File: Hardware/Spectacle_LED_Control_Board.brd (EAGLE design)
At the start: 25.4 x 55.9 mm, 43 parts, among them J3 USB-MICROB, J4 AUDIO-JACK3, J8 AUDIO-JACK3, U1 CY8C4245LQI-483, U2 3.3V, U4 SN74LVC1G66, U5 SN74LVC1G66

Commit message: Routed and ready to check
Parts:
- moved U5 0.38 mm to (16.3, 11.4)
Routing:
- net 3.3V: track 41.6 -> 20.2 mm, vias 1 -> 5
- net GND: track 44.9 -> 30.8 mm, vias 2 -> 4
- net LED: track 0.00 -> 14.0 mm, vias 0 -> 2
- net XRES: track 24.8 -> 36.2 mm
- net BTN: track 4.85 -> 6.84 mm
- net N$5: track 0.00 -> 1.66 mm
- net LED_1: track 19.5 -> 18.9 mm

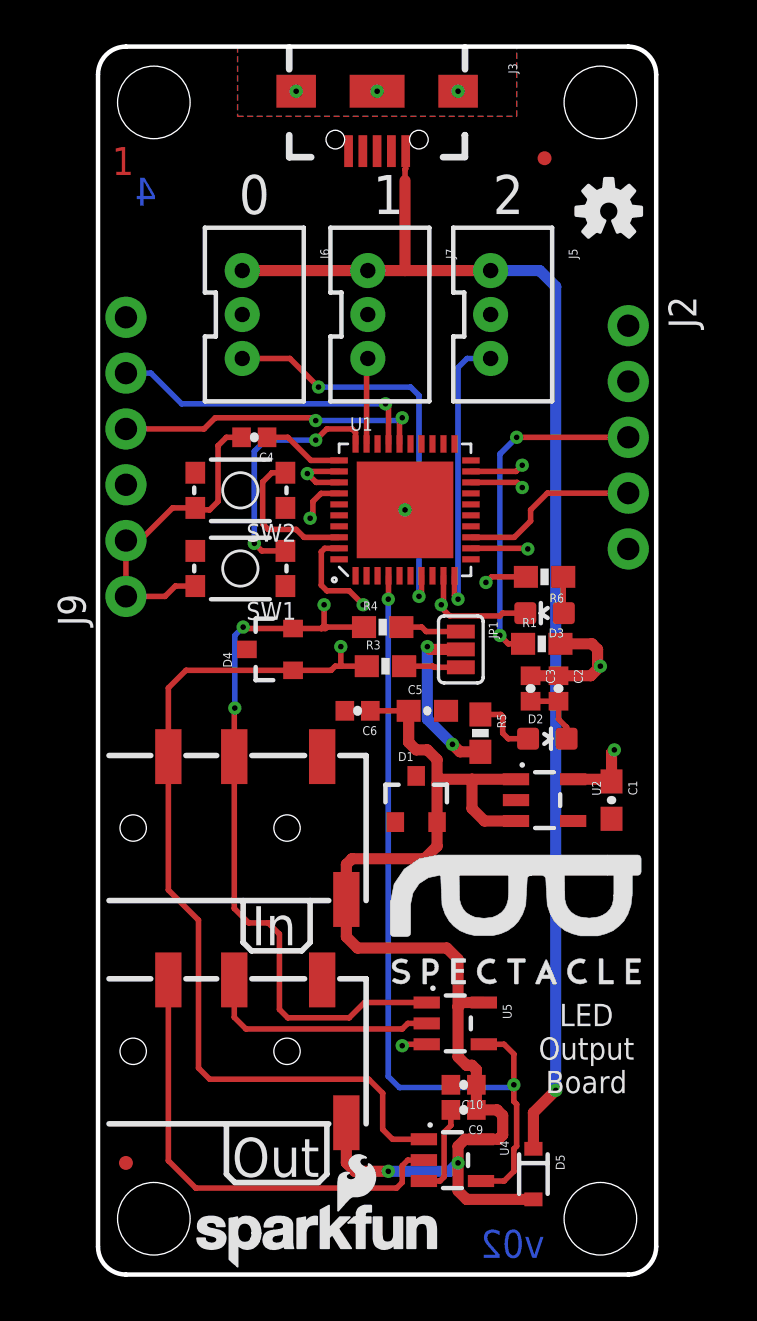
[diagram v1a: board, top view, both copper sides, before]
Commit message: moving caps
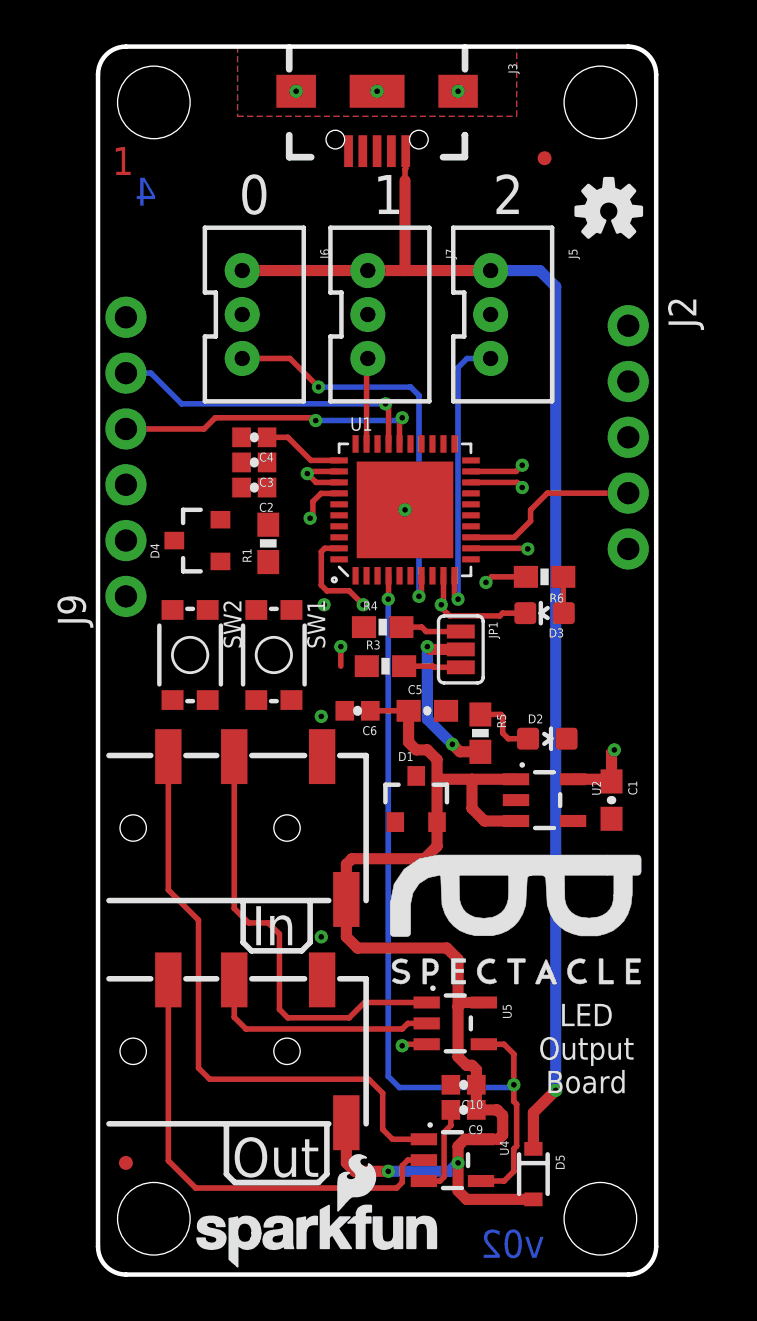
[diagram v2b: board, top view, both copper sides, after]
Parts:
- moved C2 16.6 mm to (7.11, 35.8), turned to 180 degrees
- moved C3 16.2 mm to (7.11, 37.0), turned to 180 degrees
- moved R1 13.3 mm to (7.75, 33.3), turned to 90 degrees
- moved SW2 7.83 mm to (4.19, 28.2), turned to 270 degrees
- moved D4 5.95 mm to (4.57, 33.4)
- moved SW1 4.22 mm to (8.00, 28.2), turned to 270 degrees
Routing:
- net XRES: track 36.2 -> 0.00 mm, vias 4 -> 0
- net GND: track 30.8 -> 13.0 mm, vias 4 -> 6
- net SDA: track 50.3 -> 37.5 mm, vias 4 -> 2
- net SCL: track 58.4 -> 45.8 mm
- net BTN: track 6.84 -> 0.00 mm
- net 3.3V: track 20.2 -> 14.3 mm, vias 5 -> 4

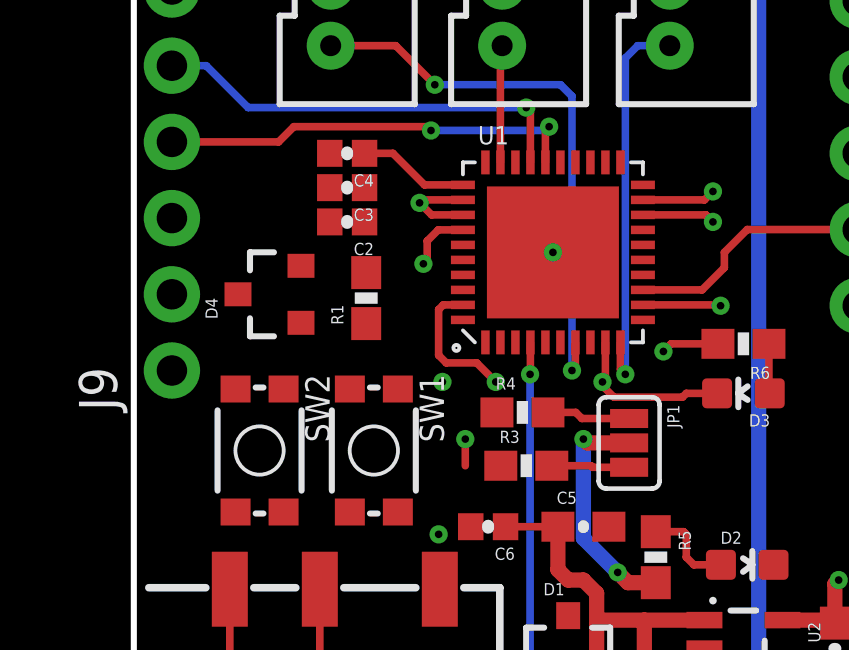
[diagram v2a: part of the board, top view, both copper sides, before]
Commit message: Moving caps
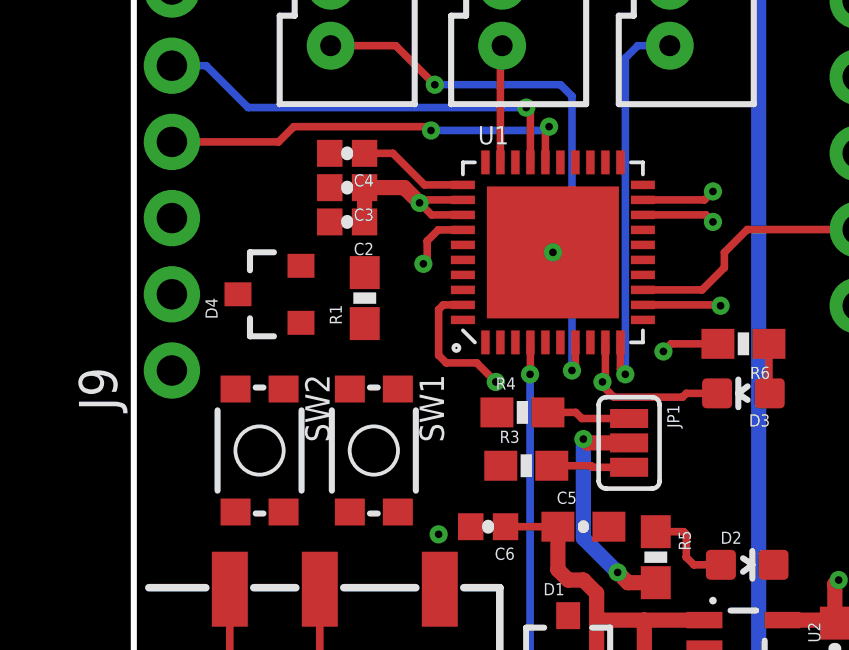
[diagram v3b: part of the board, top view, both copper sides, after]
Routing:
- net 3.3V: track 14.3 -> 17.5 mm
- net SCL: track 45.8 -> 44.9 mm, vias 2 -> 1
- net SDA: vias 2 -> 1
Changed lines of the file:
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@@
 <?xml version="1.0" encoding="utf-8"?>
 <!DOCTYPE eagle SYSTEM "eagle.dtd">
-<eagle version="7.6.0">
+<eagle version="7.3.0">
 <drawing>
 <settings>
@@
 <layers>
 <layer number="1" name="Top" color="4" fill="1" visible="yes" active="yes"/>
-<layer number="2" name="Route2" color="1" fill="3" visible="yes" active="yes"/>
-<layer number="15" name="Route15" color="4" fill="6" visible="yes" active="yes"/>
+<layer number="2" name="Route2" color="1" fill="3" visible="no" active="yes"/>
+<layer number="15" name="Route15" color="4" fill="6" visible="no" active="yes"/>
 <layer number="16" name="Bottom" color="1" fill="1" visible="yes" active="yes"/>
 <layer number="17" name="Pads" color="2" fill="1" visible="yes" active="yes"/>
@@
 <layer number="47" name="Measures" color="7" fill="1" visible="no" active="yes"/>
 <layer number="51" name="tDocu" color="6" fill="1" visible="yes" active="yes"/>
-<layer number="52" name="bDocu" color="7" fill="1" visible="no" active="yes"/>
+<layer number="52" name="bDocu" color="7" fill="1" visible="no" active="no"/>
 <layer number="48" name="Document" color="7" fill="1" visible="no" active="no"/>
 <layer number="49" name="Reference" color="7" fill="1" visible="no" active="no"/>
@@
 <attribute name="PROD_ID" value="VREG-12457" x="20.32" y="21.59" size="1.778" layer="27" font="vector" ratio="15" rot="R270" display="off"/>
 </element>
-<element name="R1" library="SparkFun-Resistors" package="0603-RES" value="10K" x="7.747" y="33.274" rot="R90">
-<attribute name="PROD_ID" value="RES-00824" x="7.747" y="33.274" size="1.778" layer="27" font="vector" ratio="15" rot="R90" display="off"/>
+<element name="R1" library="SparkFun-Resistors" package="0603-RES" value="10K" x="7.697" y="33.274" rot="R90">
+<attribute name="PROD_ID" value="RES-00824" x="7.697" y="33.274" size="1.778" layer="27" font="vector" ratio="15" rot="R90" display="off"/>
 </element>
 <element name="C1" library="SparkFun-Capacitors" package="0603-CAP" value="2.2uF" x="23.368" y="21.59" rot="R270">
@@
 <contactref element="SW1" pad="1"/>
 <contactref element="U1" pad="30"/>
-<wire x1="7.747" y1="32.424" x2="24.13" y2="38.1" width="0" layer="19" extent="1-1"/>
-<wire x1="11.72" y1="37.798" x2="7.747" y2="32.424" width="0" layer="19" extent="1-1"/>
-<wire x1="7.201" y1="30.244" x2="11.72" y2="37.798" width="0" layer="19" extent="1-1"/>
+<wire x1="11.72" y1="37.798" x2="24.13" y2="38.1" width="0" layer="19" extent="1-1"/>
+<wire x1="7.697" y1="32.424" x2="11.72" y2="37.798" width="0" layer="19" extent="1-1"/>
+<wire x1="7.201" y1="30.244" x2="7.697" y2="32.424" width="0" layer="19" extent="1-1"/>
 </signal>
 <signal name="VIN">
@@
 <wire x1="11.557" y1="35.814" x2="11.049" y2="35.306" width="0.254" layer="2"/>
 <wire x1="11.049" y1="35.306" x2="11.049" y2="28.575" width="0.254" layer="2"/>
-<via x="11.049" y="28.575" extent="1-16" drill="0.254"/>
-<wire x1="11.049" y1="28.575" x2="11.049" y2="27.686" width="0.254" layer="1"/>
-<wire x1="11.049" y1="27.686" x2="12.231" y2="27.686" width="0" layer="19" extent="1-1"/>
+<wire x1="12.231" y1="27.686" x2="11.049" y2="28.575" width="0" layer="19" extent="1-2"/>
 <wire x1="5.572" y1="32.451" x2="11.049" y2="35.306" width="0" layer="19" extent="1-2"/>
-<wire x1="3.2" y1="23.57" x2="11.049" y2="27.686" width="0" layer="19" extent="1-1"/>
+<wire x1="3.2" y1="23.57" x2="5.572" y2="32.451" width="0" layer="19" extent="1-1"/>
 </signal>
 <signal name="SDA">
@@
 <wire x1="10.795" y1="36.83" x2="10.287" y2="36.322" width="0.254" layer="2"/>
 <wire x1="10.287" y1="36.322" x2="10.287" y2="30.48" width="0.254" layer="2"/>
-<via x="10.287" y="30.48" extent="1-16" drill="0.254"/>
 <wire x1="14.9559" y1="12.38" x2="12.126" y2="12.38" width="0.254" layer="1"/>
 <wire x1="12.126" y1="12.38" x2="11.43" y2="11.684" width="0.254" layer="1"/>
@@
 <wire x1="21.6201" y1="22.54" x2="23.268" y2="22.54" width="0.508" layer="1"/>
 <wire x1="23.268" y1="22.54" x2="23.368" y2="22.44" width="0.508" layer="1"/>
-<wire x1="22.86" y1="27.686" x2="22.86" y2="27.686" width="0" layer="19" extent="1-16"/>
-<wire x1="7.747" y1="34.124" x2="22.479" y2="28.702" width="0" layer="19" extent="1-16"/>
-<wire x1="22.479" y1="28.702" x2="22.733" y2="28.448" width="0" layer="19" extent="1-16"/>
 <wire x1="16.51" y1="28.448" x2="15.113" y2="28.448" width="0.508" layer="1"/>
 <wire x1="15.113" y1="28.448" x2="14.986" y2="28.575" width="0.508" layer="1"/>
@@
 <wire x1="10.97" y1="36.048" x2="9.926" y2="36.048" width="0.254" layer="1"/>
 <wire x1="9.926" y1="36.048" x2="9.525" y2="36.449" width="0.254" layer="1"/>
-<wire x1="22.86" y1="27.686" x2="22.733" y2="28.448" width="0" layer="19" extent="1-1"/>
-<wire x1="7.692" y1="35.814" x2="7.747" y2="34.124" width="0" layer="19" extent="1-1"/>
-<wire x1="7.692" y1="36.957" x2="7.692" y2="35.814" width="0" layer="19" extent="1-1"/>
+<wire x1="7.692" y1="36.957" x2="7.692" y2="35.814" width="0.508" layer="1"/>
+<wire x1="7.692" y1="36.957" x2="9.017" y2="36.957" width="0.508" layer="1"/>
+<wire x1="9.017" y1="36.957" x2="9.525" y2="36.449" width="0.508" layer="1"/>
+<wire x1="7.692" y1="35.814" x2="7.697" y2="34.124" width="0" layer="19" extent="1-1"/>
 </signal>
 <signal name="ISO_POUR">

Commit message: ready for review!
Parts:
- moved C6 7.61 mm to (18.2, 21.5)
- moved R5 4.11 mm to (21.5, 25.3)
- moved C5 3.87 mm to (17.9, 23.1), turned to 180 degrees
- moved C1 3.68 mm to (23.4, 25.3), turned to 90 degrees
- moved C10 3.56 mm to (16.6, 12.2)
- moved D2 3.43 mm to (20.6, 27.8), turned to 90 degrees
- moved U2 1.80 mm to (22.1, 21.3)
- moved U5 1.65 mm to (16.3, 9.78)
- moved D1 0.13 mm to (14.5, 21.5)
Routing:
- net XRES: track 0.00 -> 28.2 mm, vias 0 -> 3
- net SCL: track 44.9 -> 70.8 mm, vias 1 -> 2
- net SDA: track 37.5 -> 62.7 mm, vias 1 -> 4
- net VIN: track 55.1 -> 65.6 mm
- net BTN: track 0.00 -> 10.3 mm, vias 0 -> 2
- net 3.3V: track 17.5 -> 26.1 mm, vias 4 -> 3
- net GND: track 13.0 -> 15.5 mm
- net I2C_OUT_EN: track 37.4 -> 35.9 mm
- net N$4: track 3.07 -> 1.71 mm
- net SDA_OUT: track 10.8 -> 11.3 mm
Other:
- board text added: "v03"
- board text removed: "v02"

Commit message: review edits
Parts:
- added U$2: (no value), SparkFun-Aesthetics:ORDERING_INSTRUCTIONS
- moved U$1 19.7 mm to (34.3, 35.6)
- moved FRAME1 12.0 mm to (49.5, 52.1)
- moved D5 3.74 mm to (22.9, 6.73), turned to 0 degrees
- moved C6 0.64 mm to (17.5, 21.5), turned to 0 degrees
- moved LOGO2 0.40 mm to (4.45, 0.13)
- moved C5 0.18 mm to (17.8, 23.0), turned to 0 degrees
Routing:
- net VIN: track 65.6 -> 66.8 mm
- net 5V: track 59.9 -> 59.1 mm
- net GND: vias 6 -> 8
